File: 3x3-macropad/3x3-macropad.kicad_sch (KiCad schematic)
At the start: 24 parts, among them SW1 SW_Push, U1 ATmega32U4-A, Y1 16MHz

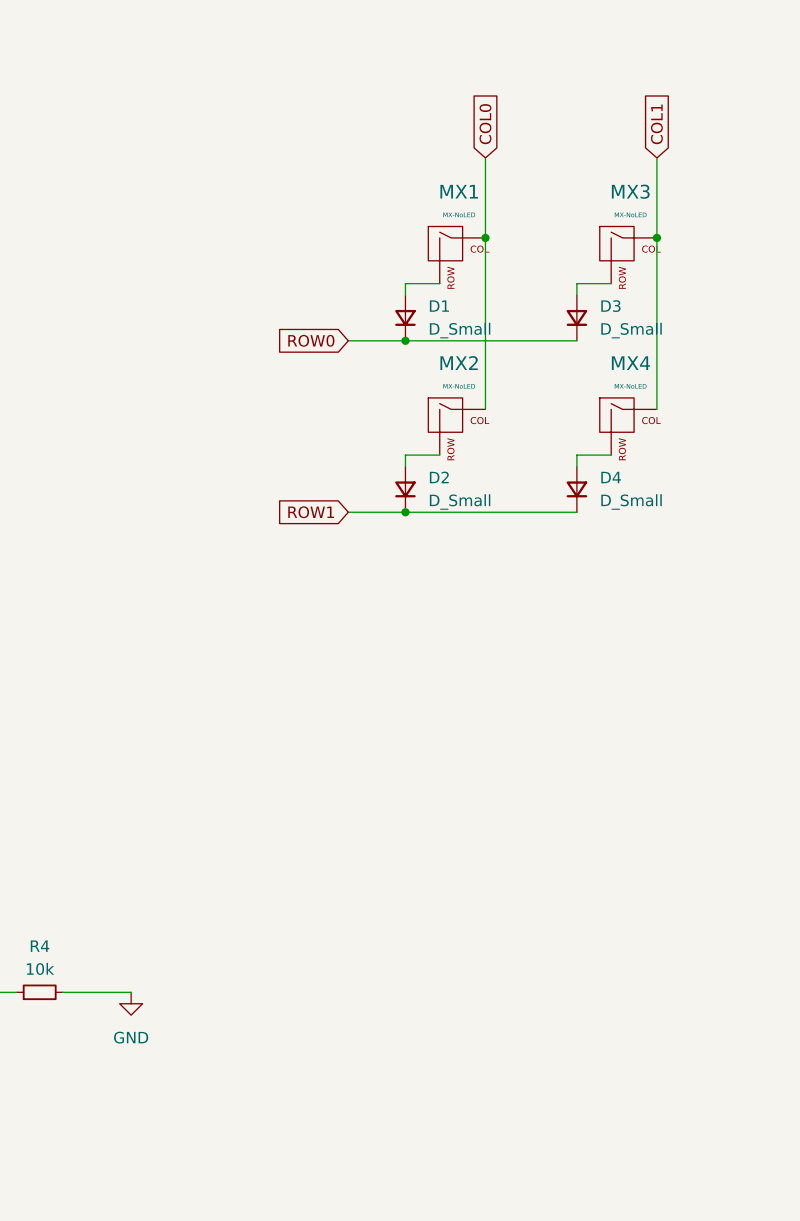
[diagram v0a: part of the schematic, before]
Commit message: start pcb layout for macropad
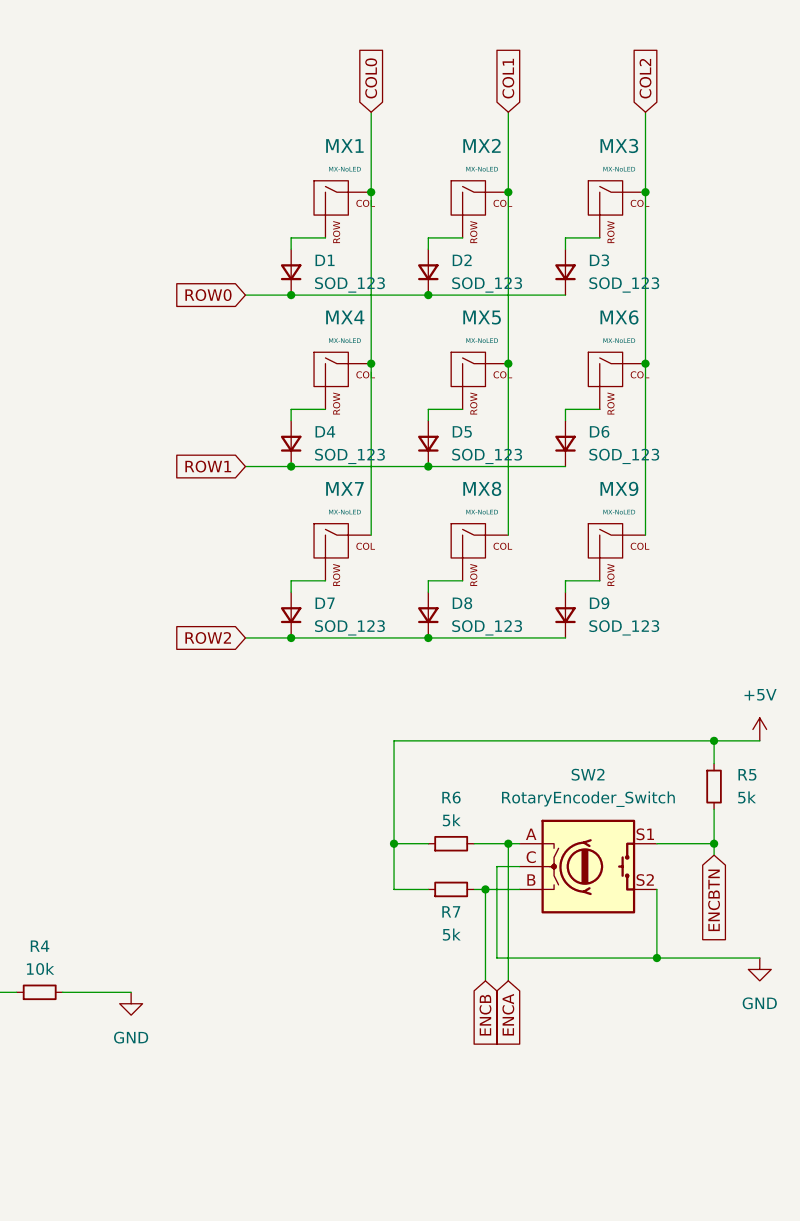
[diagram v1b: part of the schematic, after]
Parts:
- added D5, D6, D7, D8, D9: SOD_123, Diode_SMD:D_SOD-123, symbol Device:D_Small
- added MX5, MX6, MX7, MX8, MX9: MX-NoLED, MX_Alps_Hybrid:MX-1U-NoLED, symbol MX_Alps_Hybrid:MX-NoLED
- added R5, R6, R7: 5k, Resistor_SMD:R_0805_2012Metric, symbol Device:R_Small
- added SW2: RotaryEncoder_Switch, Rotary_Encoder:RotaryEncoder_Alps_EC11E-Switch_Vertical_H20mm, symbol Device:RotaryEncoder_Switch
- D1, D2, D3, D4: value D_Small -> SOD_123
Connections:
- net +5V: now also R5.1, R6.1, R7.1
- net COL0: now also MX4.1 (COL), MX7.1 (COL); no longer MX2.1 (COL)
- net COL1: now also MX2.1 (COL), MX5.1 (COL), MX8.1 (COL); no longer MX3.1 (COL), MX4.1 (COL)
- net GND: now also SW2.C, SW2.S2
- net ROW0: now also D2.1 (K)
- net ROW1: now also D5.1 (K), D6.1 (K); no longer D2.1 (K)
- new net: D5.2 (A), MX5.2 (ROW)
- new net: D8.2 (A), MX8.2 (ROW)
- new net: D6.2 (A), MX6.2 (ROW)
- new net: D9.2 (A), MX9.2 (ROW)
- new net: D7.2 (A), MX7.2 (ROW)
- new net COL2: MX3.1 (COL), MX6.1 (COL), MX9.1 (COL)
- new net ENCA: R6.2, SW2.A
- new net ENCB: R7.2, SW2.B
- new net ENCBTN: R5.2, SW2.S1
- new net ROW2: D7.1 (K), D8.1 (K), D9.1 (K)

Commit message: first attempt routing 3x3
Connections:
- net COL0: now also U1.29 (PB5)
- net COL1: now also U1.28 (PB4)
- net COL2: now also U1.27 (PD7)
- net ENCA: now also U1.30 (PB6)
- net ENCB: now also U1.31 (PC6)
- net ENCBTN: now also U1.32 (PC7)
- net ROW0: now also U1.26 (PD6)
- net ROW1: now also U1.25 (PD4)
- net ROW2: now also U1.22 (PD5)
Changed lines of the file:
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@@
+    )
+  )
+  (global_label "ROW0" (shape input) (at 151.13 114.3 0) (fields_autoplaced)
+    (effects (font (size 1.27 1.27)) (justify left))
+    (property "Intersheetrefs" "${INTERSHEET_REFS}" (at 159.2972 114.3 0)
+      (effects (font (size 1.27 1.27)) (justify left) hide)
     )
   )
@@
     (effects (font (size 1.27 1.27)) (justify left))
     (property "Intersheetrefs" "${INTERSHEET_REFS}" (at 227.33 16.3861 90)
+      (effects (font (size 1.27 1.27)) (justify left) hide)
+    )
+  )
+  (global_label "COL1" (shape input) (at 151.13 78.74 0) (fields_autoplaced)
+    (effects (font (size 1.27 1.27)) (justify left))
+    (property "Intersheetrefs" "${INTERSHEET_REFS}" (at 158.8739 78.74 0)
+      (effects (font (size 1.27 1.27)) (justify left) hide)
+    )
+  )
+  (global_label "ENCBTN" (shape input) (at 151.13 93.98 0) (fields_autoplaced)
+    (effects (font (size 1.27 1.27)) (justify left))
+    (property "Intersheetrefs" "${INTERSHEET_REFS}" (at 161.3534 93.98 0)
+      (effects (font (size 1.27 1.27)) (justify left) hide)
+    )
+  )
+  (global_label "COL2" (shape input) (at 151.13 116.84 0) (fields_autoplaced)
+    (effects (font (size 1.27 1.27)) (justify left))
+    (property "Intersheetrefs" "${INTERSHEET_REFS}" (at 158.8739 116.84 0)
+      (effects (font (size 1.27 1.27)) (justify left) hide)
+    )
+  )
+  (global_label "COL0" (shape input) (at 151.13 81.28 0) (fields_autoplaced)
+    (effects (font (size 1.27 1.27)) (justify left))
+    (property "Intersheetrefs" "${INTERSHEET_REFS}" (at 158.8739 81.28 0)
+      (effects (font (size 1.27 1.27)) (justify left) hide)
+    )
+  )
+  (global_label "ENCA" (shape input) (at 151.13 83.82 0) (fields_autoplaced)
+    (effects (font (size 1.27 1.27)) (justify left))
+    (property "Intersheetrefs" "${INTERSHEET_REFS}" (at 158.8739 83.82 0)
       (effects (font (size 1.27 1.27)) (justify left) hide)
     )
@@
     (property "Intersheetrefs" "${INTERSHEET_REFS}" (at 212.09 128.3939 90)
       (effects (font (size 1.27 1.27)) (justify right) hide)
+    )
+  )
+  (global_label "ROW2" (shape input) (at 151.13 111.76 0) (fields_autoplaced)
+    (effects (font (size 1.27 1.27)) (justify left))
+    (property "Intersheetrefs" "${INTERSHEET_REFS}" (at 159.2972 111.76 0)
+      (effects (font (size 1.27 1.27)) (justify left) hide)
     )
   )
@@
     (effects (font (size 1.27 1.27)) (justify left))
     (property "Intersheetrefs" "${INTERSHEET_REFS}" (at 196.85 16.3861 90)
+      (effects (font (size 1.27 1.27)) (justify left) hide)
+    )
+  )
+  (global_label "ENCB" (shape input) (at 151.13 91.44 0) (fields_autoplaced)
+    (effects (font (size 1.27 1.27)) (justify left))
+    (property "Intersheetrefs" "${INTERSHEET_REFS}" (at 159.0553 91.44 0)
       (effects (font (size 1.27 1.27)) (justify left) hide)
     )
@@
     )
   )
+  (global_label "ROW1" (shape input) (at 151.13 109.22 0) (fields_autoplaced)
+    (effects (font (size 1.27 1.27)) (justify left))
+    (property "Intersheetrefs" "${INTERSHEET_REFS}" (at 159.2972 109.22 0)
+      (effects (font (size 1.27 1.27)) (justify left) hide)
+    )
+  )

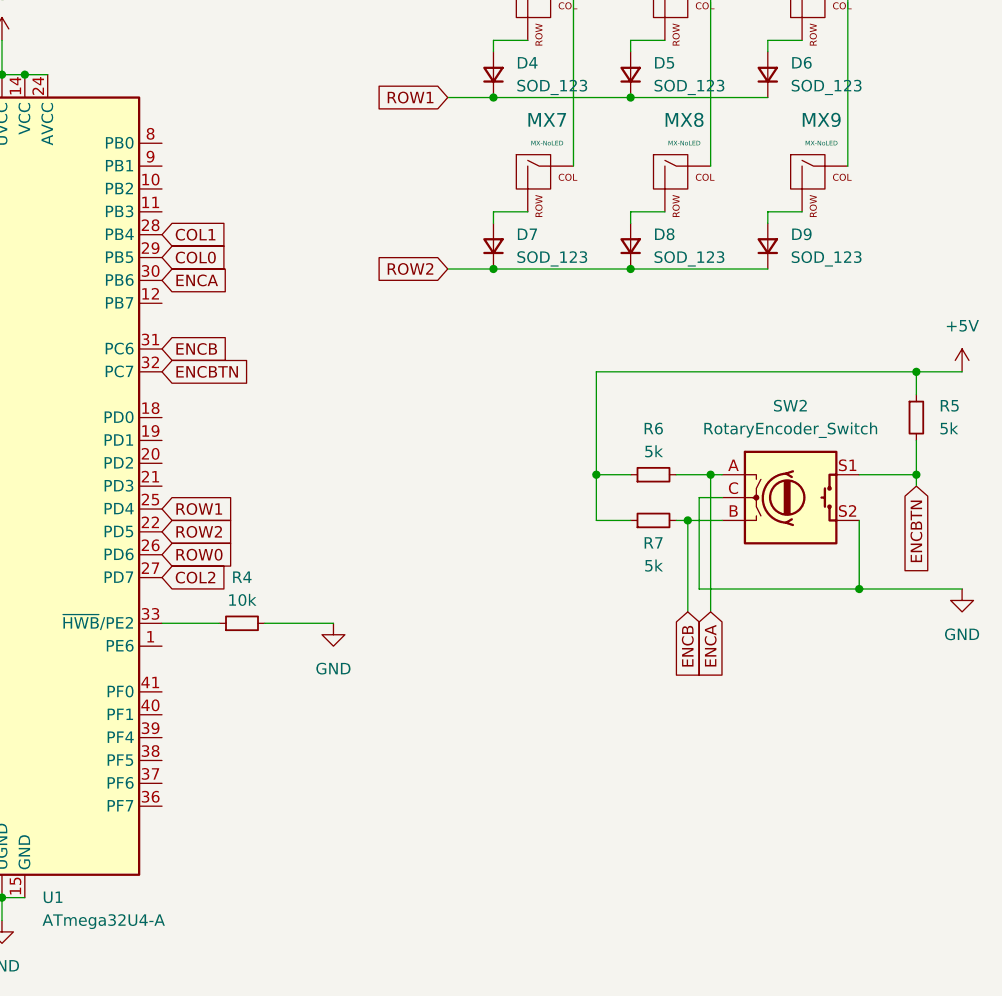
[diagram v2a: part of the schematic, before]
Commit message: redo pcb routing (better)
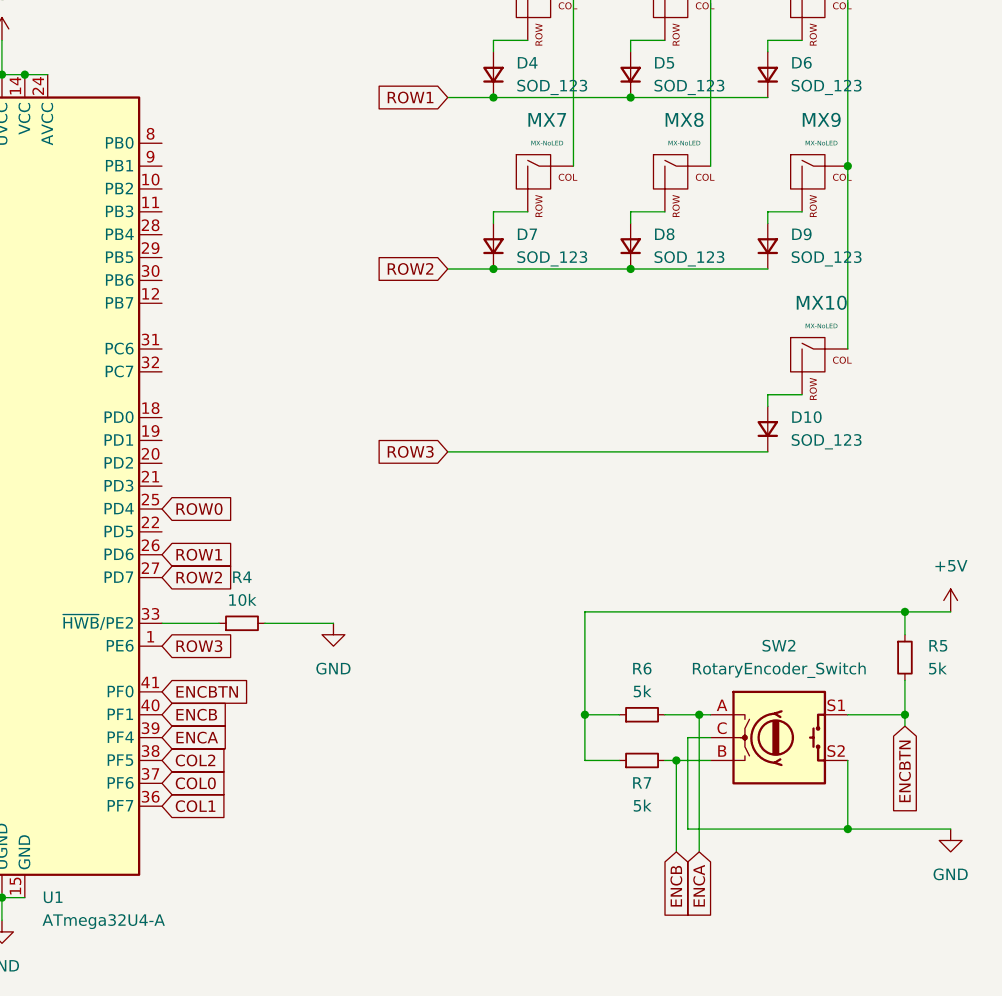
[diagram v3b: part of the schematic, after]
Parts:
- added D10: SOD_123, Diode_SMD:D_SOD-123, symbol Device:D_Small
- added MX10: MX-NoLED, MX_Alps_Hybrid:MX-1U-NoLED, symbol MX_Alps_Hybrid:MX-NoLED
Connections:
- net COL0: now also U1.37 (PF6); no longer U1.29 (PB5)
- net COL1: now also U1.36 (PF7); no longer U1.28 (PB4)
- net COL2: now also U1.38 (PF5), MX10.1 (COL); no longer U1.27 (PD7)
- net ENCA: now also U1.39 (PF4); no longer U1.30 (PB6)
- net ENCB: now also U1.40 (PF1); no longer U1.31 (PC6)
- net ENCBTN: now also U1.41 (PF0); no longer U1.32 (PC7)
- net ROW0: now also U1.25 (PD4); no longer U1.26 (PD6)
- net ROW1: now also U1.26 (PD6); no longer U1.25 (PD4)
- net ROW2: now also U1.27 (PD7); no longer U1.22 (PD5)
- net ROW3: now reaches U1.1 (PE6)
- net ROW3: now also D10.1 (K)
- new net: D10.2 (A), MX10.2 (ROW)
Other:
- moved on the sheet: R5, R6, R7, SW2

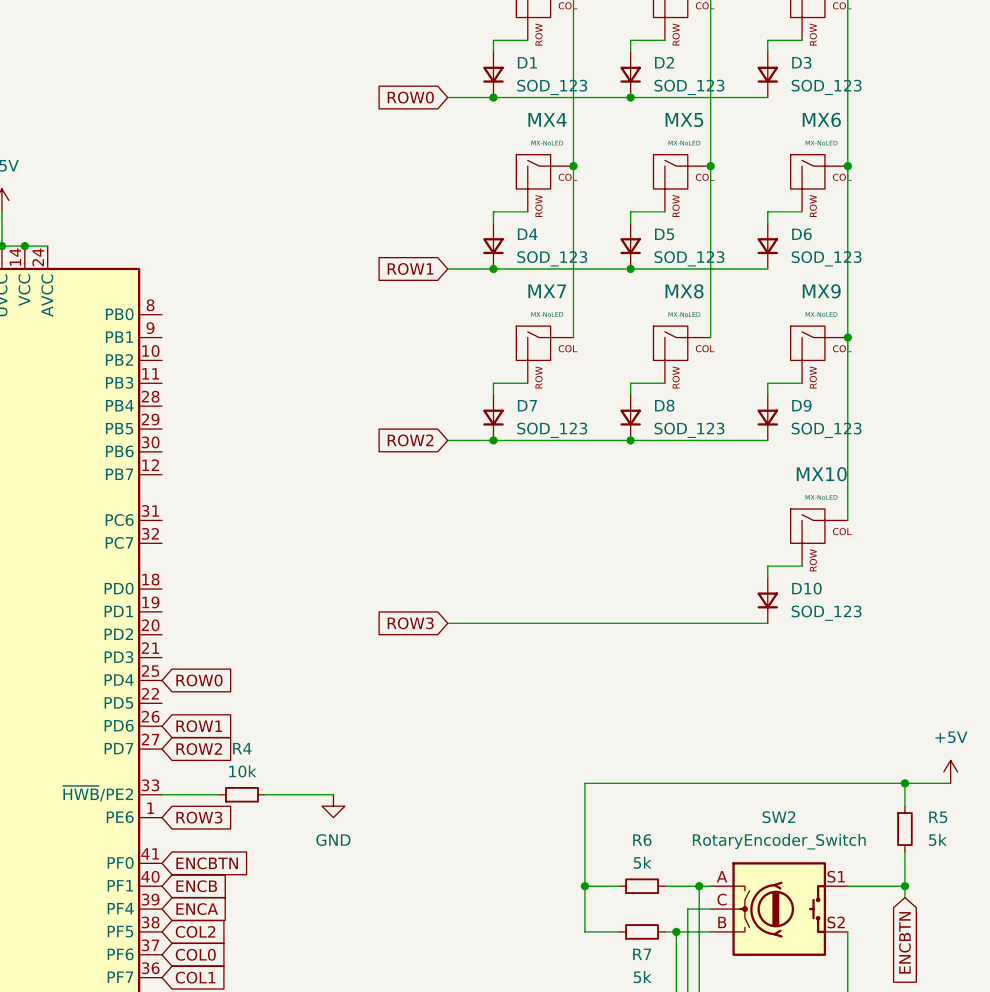
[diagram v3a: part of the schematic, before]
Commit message: resized 3x3, readied for export to jlcpcb
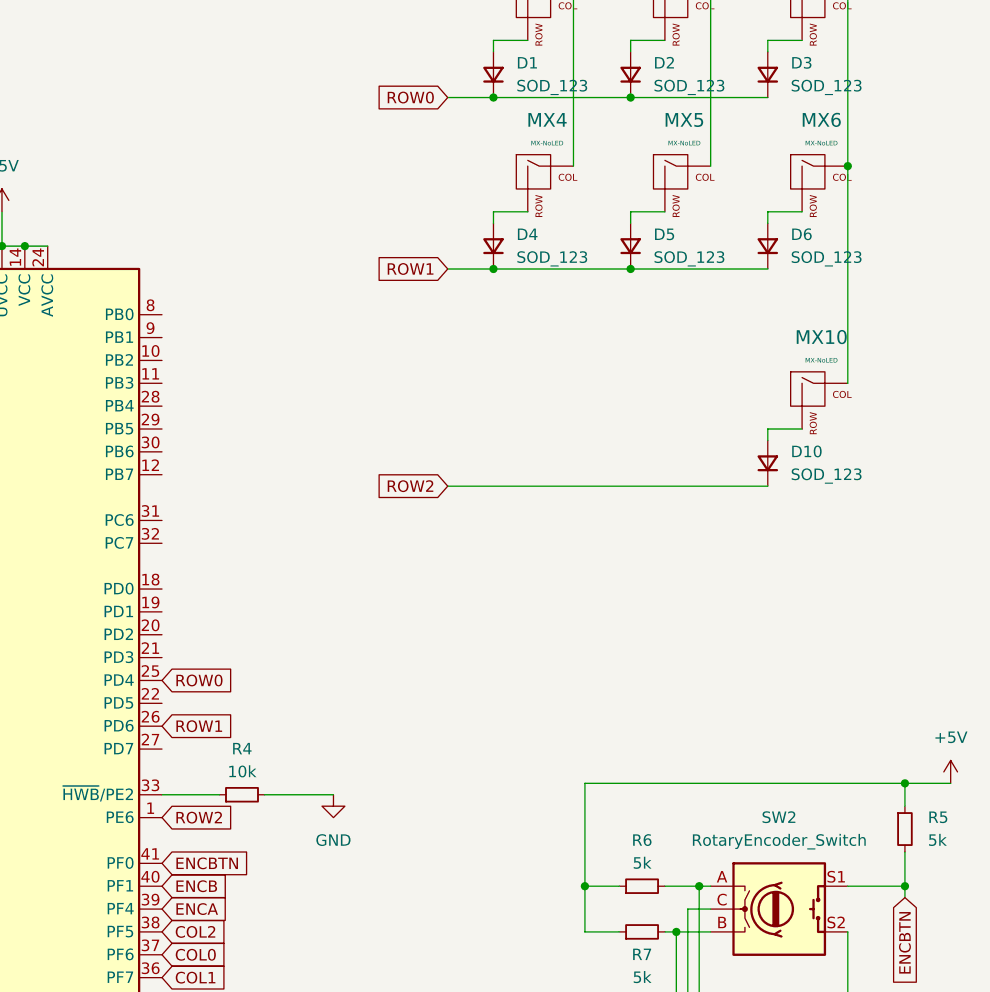
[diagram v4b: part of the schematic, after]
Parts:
- removed D7, D8, D9: SOD_123, Diode_SMD:D_SOD-123, symbol Device:D_Small
- removed MX7, MX8, MX9: MX-NoLED, MX_Alps_Hybrid:MX-1U-NoLED, symbol MX_Alps_Hybrid:MX-NoLED
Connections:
- net ROW3 is gone; now on net ROW2: D10.1 (K), U1.1 (PE6)
- net ROW2: no longer U1.27 (PD7)
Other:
- moved on the sheet: D10, MX10

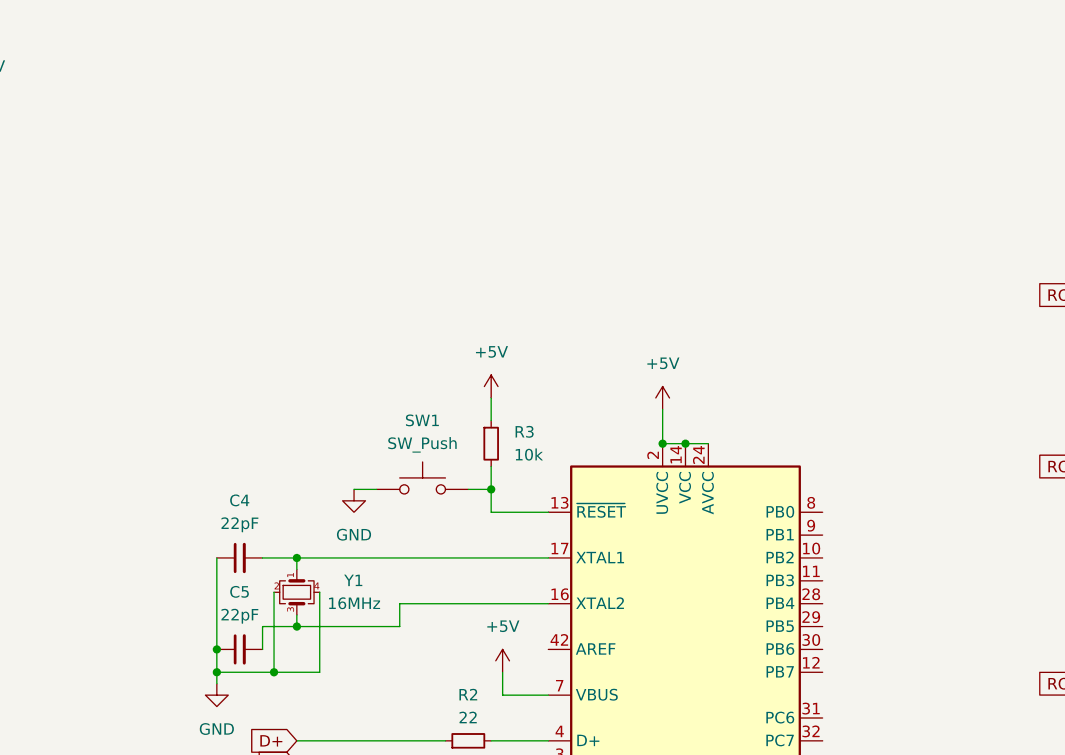
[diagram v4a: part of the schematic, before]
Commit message: add isp flashing breakout
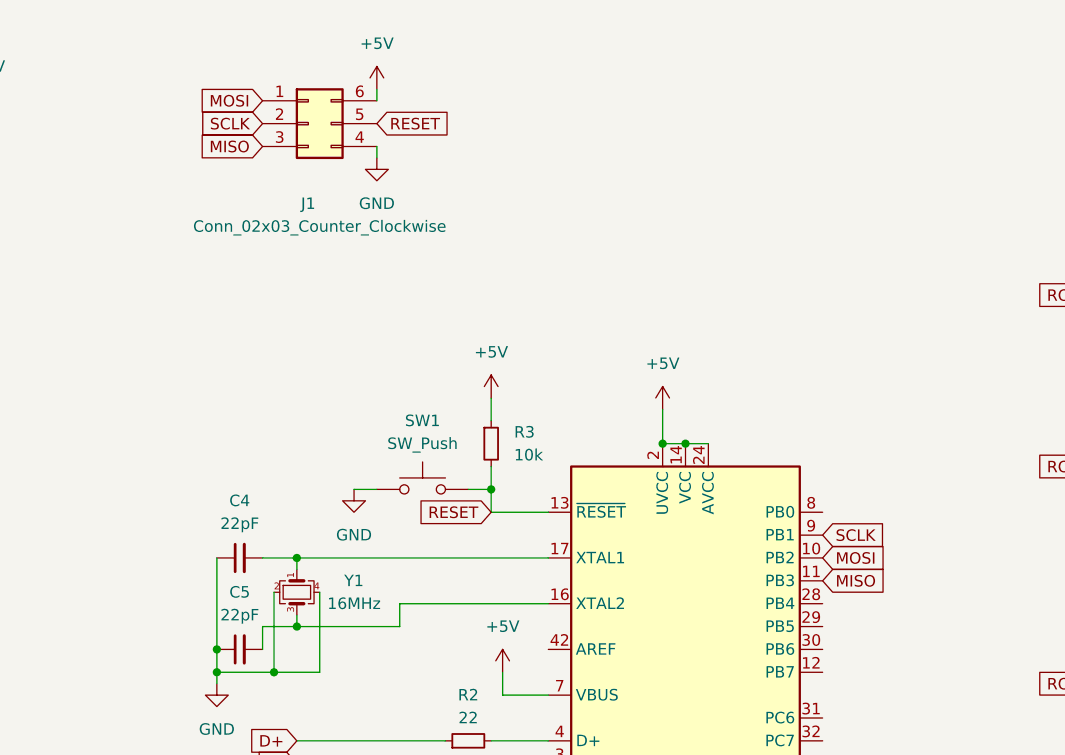
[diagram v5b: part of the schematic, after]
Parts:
- added J1: Conn_02x03_Counter_Clockwise, Connector_PinHeader_1.27mm:PinHeader_2x03_P1.27mm_Horizontal, symbol Connector_Generic:Conn_02x03_Counter_Clockwise
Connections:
- net +5V: now also J1.6 (Pin_6)
- net GND: now also J1.4 (Pin_4)
- net RESET: now reaches R3.2, SW1.2, U1.13 (~{RESET})
- net RESET: now also J1.5 (Pin_5)
- net MOSI: now reaches U1.10 (PB2)
- net MOSI: now also J1.1 (Pin_1)
- net MISO: now reaches U1.11 (PB3)
- net MISO: now also J1.3 (Pin_3)
- net SCLK: now reaches U1.9 (PB1)
- net SCLK: now also J1.2 (Pin_2)
